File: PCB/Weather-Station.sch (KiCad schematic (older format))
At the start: 10 parts, among them J1 Biruta, J2 Power, J3 BH1750-FVI, J4 BME280, J5 Pluviometro, J6 Anamometro, U1 NodeMCU1.0(ESP-12E)

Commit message: Adicionando Gerber
Signed-off-by: Gustavo Costa <gustavocosta@ic.ufal.br>
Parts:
- J6: value Anamometro -> Anemometro
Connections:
- net labels added: +3.3V, +5V, GND
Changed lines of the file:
@@
 P 8150 3050
 F 0 "J6" H 8150 3150 50  0000 C CNN
-F 1 "Anamometro" H 8150 2850 50  0000 C CNN
+F 1 "Anemometro" H 8150 2850 50  0000 C CNN
 F 2 "Terminal_Blocks:TerminalBlock_Pheonix_MPT-2.54mm_2pol" H 8150 3050 50  0001 C CNN
 F 3 "" H 8150 3050 50  0001 C CNN
@@
 $EndComp
 Wire Wire Line
-	4900 3650 4250 3650
-Wire Wire Line
-	4250 3650 4250 2750
-Wire Wire Line
 	4250 2750 4000 2750
 Wire Wire Line
@@
 	6600 3950 6500 3950
 Wire Wire Line
-	6600 1400 6600 3950
-Wire Wire Line
 	6600 2950 7350 2950
 Wire Wire Line
@@
 Wire Wire Line
 	7100 3450 7100 3150
-Wire Wire Line
-	7950 1000 6700 1000
 Connection ~ 6700 1700
 Wire Wire Line
@@
 	7950 1200 6900 1200
 Connection ~ 6900 2000
-Wire Wire Line
-	7950 1400 6600 1400
 Connection ~ 6600 1800
 NoConn ~ 7950 1300
 Wire Wire Line
 	4550 3100 4550 3550
-Wire Wire Line
-	4550 3550 4900 3550
 NoConn ~ 4900 2750
 NoConn ~ 4900 2850
@@
 $Comp
 L PWR_FLAG #FLG01
-U 1 1 5A5912D8
-P 4350 3950
-F 0 "#FLG01" H 4350 4025 50  0001 C CNN
-F 1 "PWR_FLAG" H 4350 4100 50  0000 C CNN
-F 2 "" H 4350 3950 50  0001 C CNN
-F 3 "" H 4350 3950 50  0001 C CNN
-	1    4350 3950
-	1    0    0    -1
-$EndComp
-Wire Wire Line
-	4000 3950 4900 3950
-Connection ~ 4350 3950
-$Comp
-L PWR_FLAG #FLG02
 U 1 1 5A5913B0
 P 4350 4050
-F 0 "#FLG02" H 4350 4125 50  0001 C CNN
+F 0 "#FLG01" H 4350 4125 50  0001 C CNN
 F 1 "PWR_FLAG" H 4350 4200 50  0000 C CNN
 F 2 "" H 4350 4050 50  0001 C CNN
@@
 	-1   0    0    1
 $EndComp
-Wire Wire Line
-	4000 4050 4900 4050
-Connection ~ 4350 4050
 $Comp
 L R R1
@@
 Connection ~ 7350 3150
 Connection ~ 7350 2650
+$Comp
+L GND #PWR02
+U 1 1 5A5CDF65
+P 4700 3950
+F 0 "#PWR02" H 4700 3700 50  0001 C CNN
+F 1 "GND" H 4700 3800 50  0000 C CNN
+F 2 "" H 4700 3950 50  0001 C CNN
+F 3 "" H 4700 3950 50  0001 C CNN
+	1    4700 3950
+	-1   0    0    1
+$EndComp
+$Comp
+L GND #PWR03
+U 1 1 5A5CDF8D
+P 4700 3550
+F 0 "#PWR03" H 4700 3300 50  0001 C CNN
+F 1 "GND" H 4700 3400 50  0000 C CNN
+F 2 "" H 4700 3550 50  0001 C CNN
+F 3 "" H 4700 3550 50  0001 C CNN
+	1    4700 3550
+	-1   0    0    1
+$EndComp
+Wire Wire Line
+	4550 3550 4900 3550
+Connection ~ 4700 3550
+$Comp
+L PWR_FLAG #FLG04
+U 1 1 5A5912D8
+P 4350 3950
+F 0 "#FLG04" H 4350 4025 50  0001 C CNN
+F 1 "PWR_FLAG" H 4350 4100 50  0000 C CNN
+F 2 "" H 4350 3950 50  0001 C CNN
+F 3 "" H 4350 3950 50  0001 C CNN
+	1    4350 3950
+	1    0    0    -1
+$EndComp
+Wire Wire Line
+	4000 3950 4900 3950
+Connection ~ 4350 3950
+Connection ~ 4700 3950
+$Comp
+L GND #PWR05
+U 1 1 5A5CE28B
+P 6600 1400
+F 0 "#PWR05" H 6600 1150 50  0001 C CNN
+F 1 "GND" H 6600 1250 50  0000 C CNN
+F 2 "" H 6600 1400 50  0001 C CNN
+F 3 "" H 6600 1400 50  0001 C CNN
+	1    6600 1400
+	0    1    1    0
+$EndComp
+Wire Wire Line
+	6600 1400 6600 3950
+Wire Wire Line
+	7950 1400 6600 1400
+$Comp
+L +3.3V #PWR06
+U 1 1 5A5CE575
+P 4400 3650
+F 0 "#PWR06" H 4400 3500 50  0001 C CNN
+F 1 "+3.3V" H 4400 3790 50  0000 C CNN
+F 2 "" H 4400 3650 50  0001 C CNN
+F 3 "" H 4400 3650 50  0001 C CNN
+	1    4400 3650
+	1    0    0    -1
+$EndComp
+Wire Wire Line
+	4250 3650 4900 3650
+Connection ~ 4400 3650
+$Comp
+L +3.3V #PWR07
+U 1 1 5A5CE693
+P 6700 1000
+F 0 "#PWR07" H 6700 850 50  0001 C CNN
+F 1 "+3.3V" H 6700 1140 50  0000 C CNN
+F 2 "" H 6700 1000 50  0001 C CNN
+F 3 "" H 6700 1000 50  0001 C CNN
+	1    6700 1000
+	0    -1   -1   0
+$EndComp
+Wire Wire Line
+	7950 1000 6700 1000
+$Comp
+L +5V #PWR08
+U 1 1 5A5CE7AA
+P 4700 4050
+F 0 "#PWR08" H 4700 3900 50  0001 C CNN
+F 1 "+5V" H 4700 4190 50  0000 C CNN
+F 2 "" H 4700 4050 50  0001 C CNN
+F 3 "" H 4700 4050 50  0001 C CNN
+	1    4700 4050
+	-1   0    0    1
+$EndComp
+Wire Wire Line
+	4000 4050 4900 4050
+Connection ~ 4350 4050
+Connection ~ 4700 4050
+$Comp
+L PWR_FLAG #FLG09
+U 1 1 5A5CE960
+P 4250 3300
+F 0 "#FLG09" H 4250 3375 50  0001 C CNN
+F 1 "PWR_FLAG" H 4250 3450 50  0000 C CNN
+F 2 "" H 4250 3300 50  0001 C CNN
+F 3 "" H 4250 3300 50  0001 C CNN
+	1    4250 3300
+	0    -1   -1   0
+$EndComp
+Wire Wire Line
+	4250 2750 4250 3650
+Connection ~ 4250 3300
 $EndSCHEMATC

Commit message: Refazendo PCB
Signed-off-by: Gustavo Costa <gustavocosta@ic.ufal.br>
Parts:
- removed U1: NodeMCU1.0(ESP-12E), ESP8266_l2:NodeMCU1.0(12-E), symbol NodeMCU1.0(ESP-12E)
- added C1: 100nF, Capacitors_SMD:C_0805, symbol C
- added J7: FTDI, Pin_Headers:Pin_Header_Straight_1x04_Pitch2.54mm, symbol Conn_01x04
- added R4, R5, R6, R7, R8: 10K, Resistors_SMD:R_0805, symbol R
- added SW1: SW_Push_SPDT, Buttons_Switches_ThroughHole:SW_Micro_SPST, symbol SW_Push_SPDT
- added SW2: SW_Push, Buttons_Switches_THT:SW_PUSH_6mm, symbol SW_Push
- added SW3: SW_DIP_x01, Buttons_Switches_ThroughHole:SW_Micro_SPST, symbol SW_DIP_x01
- added U1: AP1117-33, TO_SOT_Packages_SMD:SOT-223-3_TabPin2, symbol AP1117-33
- added U2: ESP-12E, ESP8266:ESP-12E, symbol ESP-12E
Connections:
- net labels added: RXD, TXD
- net labels removed: +5V
- wire segments 38 -> 89
- no-connect marks 20 -> 9
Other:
- moved on the sheet: J1, J2, J3, J4, J5, J6, R1, R2, R3

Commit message: Ajustando os valores da biruta
Signed-off-by: Gustavo Costa <gustavocosta@ic.ufal.br>
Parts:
- U1: footprint TO_SOT_Packages_SMD:SOT-223-3_TabPin2 -> TO_SOT_Packages_SMD:SOT-223
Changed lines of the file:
@@
 F 0 "U1" H 2000 2775 50  0000 C CNN
 F 1 "AP1117-33" H 2150 2775 50  0000 L CNN
-F 2 "TO_SOT_Packages_SMD:SOT-223-3_TabPin2" H 2150 2850 50  0001 C CNN
+F 2 "TO_SOT_Packages_SMD:SOT-223" H 2150 2850 50  0001 C CNN
 F 3 "" H 2250 2400 50  0001 C CNN
 	1    2150 2650

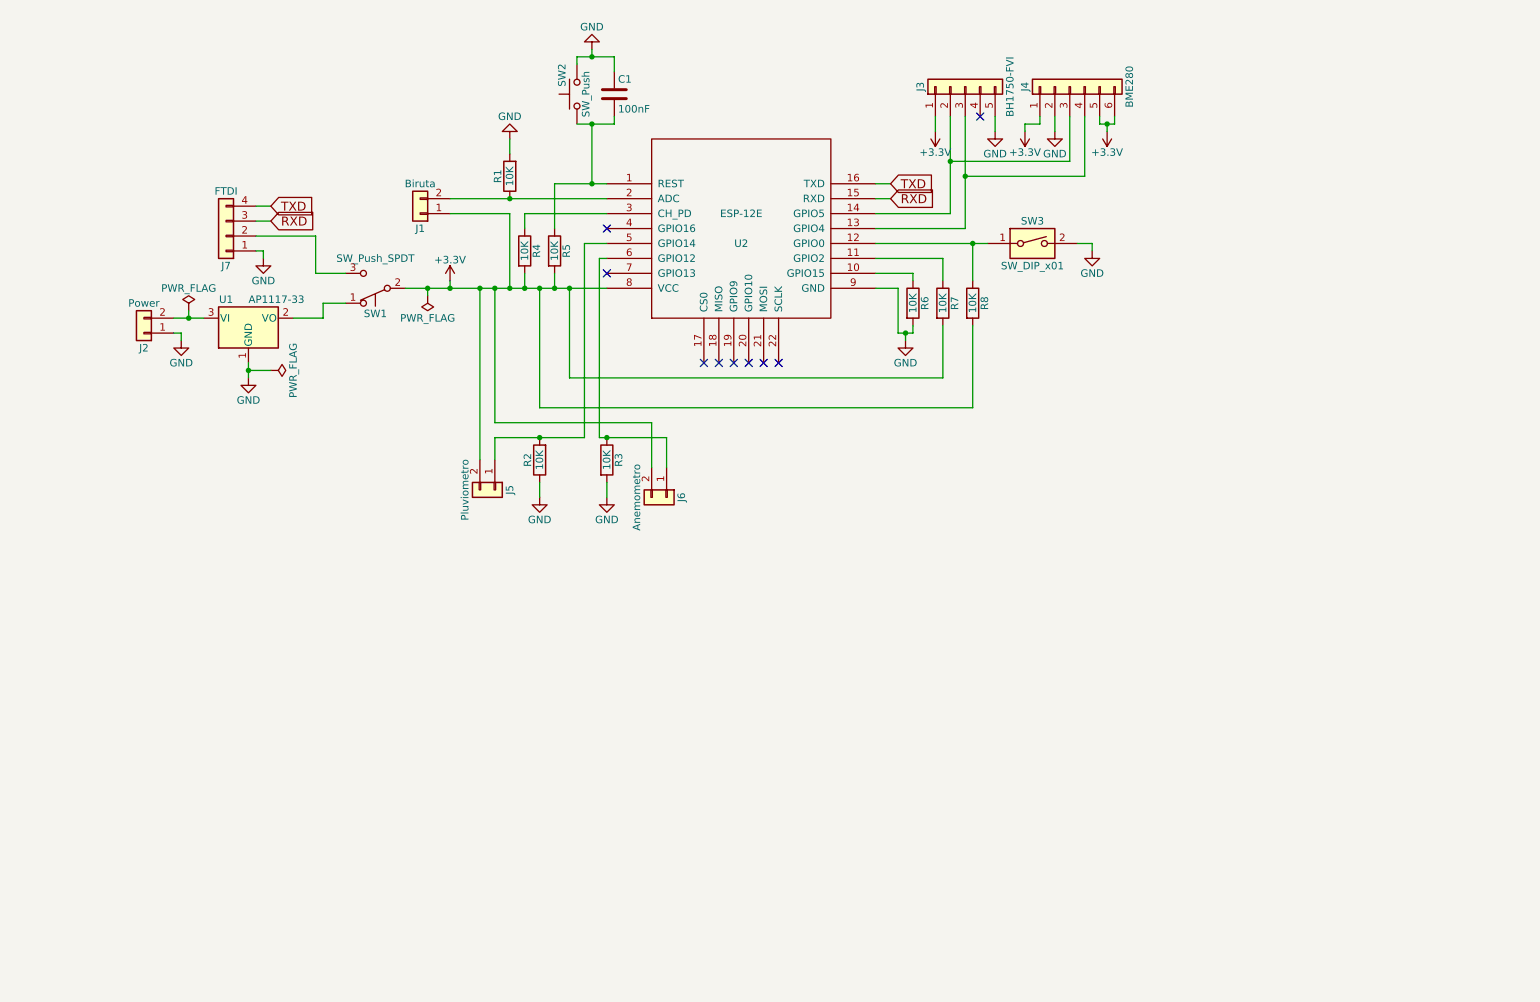
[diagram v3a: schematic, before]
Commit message: Iniciada a PCB com ESP32 devkit
Signed-off-by: Gustavo Costa <gustavocosta@ic.ufal.br>
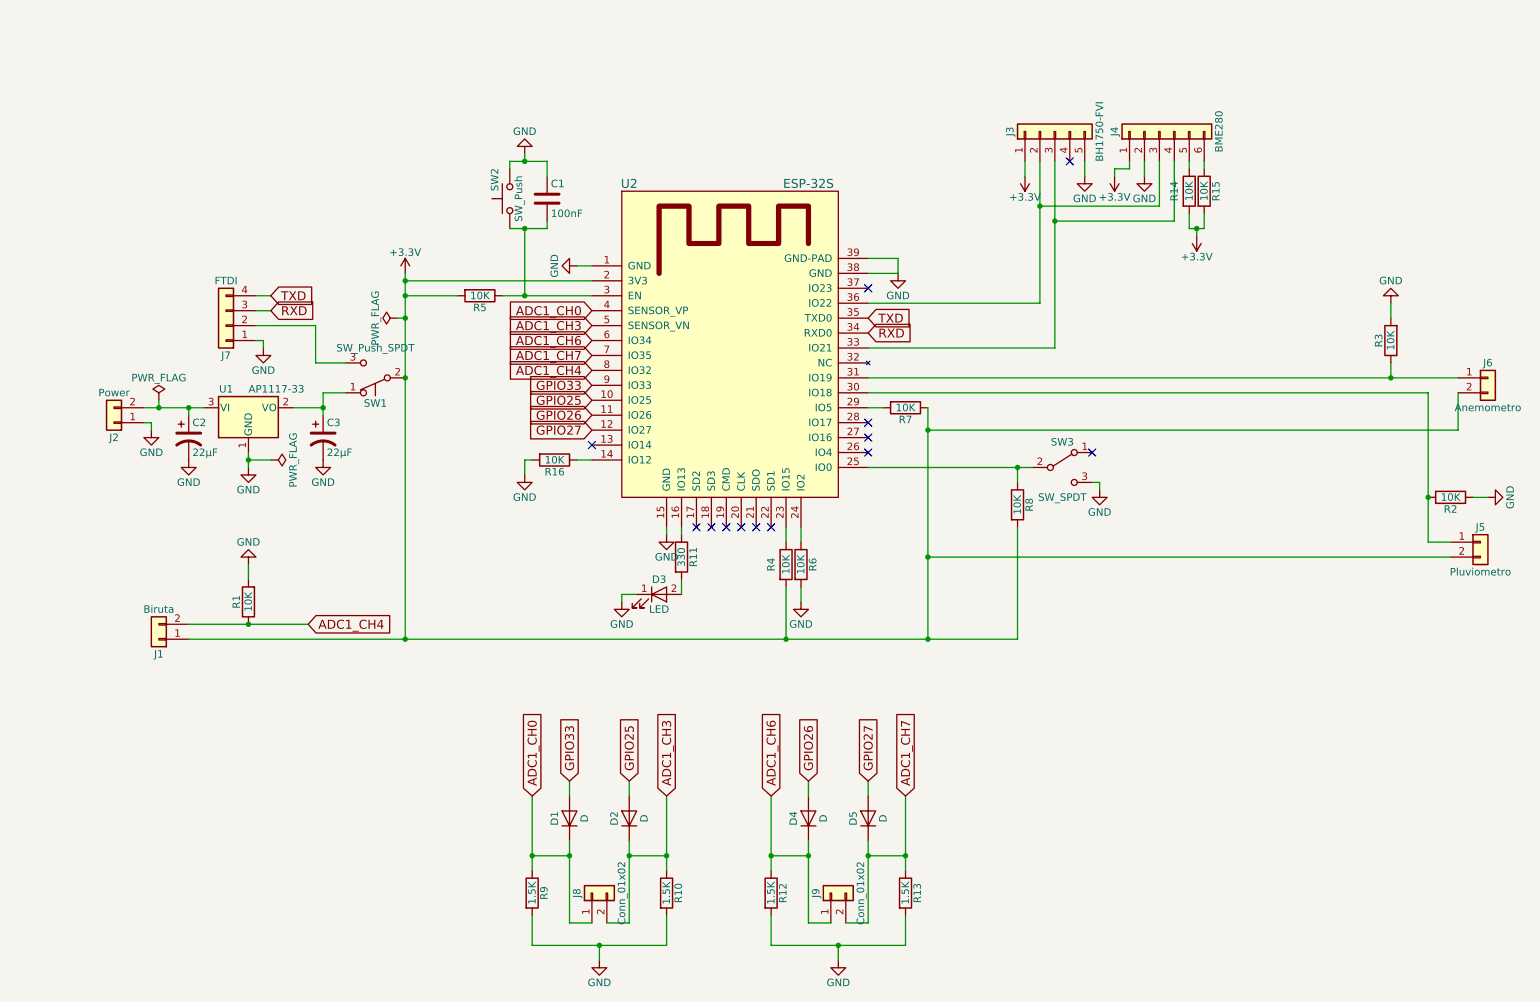
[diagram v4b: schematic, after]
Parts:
- removed SW3: SW_DIP_x01, Buttons_Switches_ThroughHole:SW_Micro_SPST, symbol SW_DIP_x01
- removed U2: ESP-12E, ESP8266:ESP-12E, symbol ESP-12E
- added C2, C3: 22μF, Capacitors_SMD:CP_Elec_6.3x7.7, symbol CP1
- added D1, D2, D4, D5: D, Diodes_SMD:D_SOD-123, symbol D
- added D3: LED, LEDs:LED_0805, symbol LED
- added J8, J9: Conn_01x02, TerminalBlock_Phoenix:TerminalBlock_Phoenix_MPT-2.54mm_2pol, symbol Conn_01x02
- added R10, R12, R13, R9: 1.5K, Resistors_SMD:R_0805, symbol R
- added R11: 330, Resistors_SMD:R_0805, symbol R
- added R14, R15, R16: 10K, Resistors_SMD:R_0805, symbol R
- added SW3: SW_SPDT, Buttons_Switches_ThroughHole:SW_Micro_SPST, symbol SW_SPDT
- added U2: ESP-32S, MPPT_Library:ESP32-WROOM, symbol ESP-32S
- J1, J2, J5, J6: footprint Terminal_Blocks:TerminalBlock_Pheonix_MPT-2.54mm_2pol -> TerminalBlock_Phoenix:TerminalBlock_Phoenix_MPT-2.54mm_2pol
- J3: footprint Terminal_Blocks:TerminalBlock_Pheonix_MPT-2.54mm_5pol -> TerminalBlock_Phoenix:TerminalBlock_Phoenix_MPT-2.54mm_5pol
- J4: footprint Terminal_Blocks:TerminalBlock_Pheonix_MPT-2.54mm_6pol -> TerminalBlock_Phoenix:TerminalBlock_Phoenix_MPT-2.54mm_6pol
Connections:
- net +3V3: now also R7.1, R14.2, R15.2, U2.2 (3V3); no longer J4.5 (Pin_5), J4.6 (Pin_6), R7.2
- net GND: now also C2.2, C3.2, D3.1 (K), R10.2, R12.2, R13.2, R16.2, R9.2, SW3.3 (C), U2.1 (GND), U2.15 (GND), U2.38 (GND), U2.39 (GND-PAD)
- net RXD: now also U2.34 (RXD0)
- net TXD: now also U2.35 (TXD0)
- net at J6.1 (Pin_1), R3.1: now also U2.31 (IO19)
- net at J5.1 (Pin_1), R2.2: now also U2.30 (IO18)
- net ADC1_CH4: now reaches J1.2 (Pin_2), R1.1
- net ADC1_CH4: now also U2.8 (IO32)
- net at J3.2 (Pin_2), J4.3 (Pin_3): now also U2.36 (IO22)
- net at J3.3 (Pin_3), J4.4 (Pin_4): now also U2.33 (IO21)
- net at J2.2 (Pin_2), U1.3 (VI): now also C2.1
- net at C1.2, R5.1, SW2.1: now also U2.3 (EN)
- net at R6.1: now also U2.24 (IO2)
- net at R8.1: now also SW3.2 (B), U2.25 (IO0)
- net at R4.1: now also U2.23 (IO15)
- net at SW1.1 (A), U1.2 (VO): now also C3.1
- new net: J4.5 (Pin_5), R14.1
- new net: J4.6 (Pin_6), R15.1
- new net: R7.2, U2.29 (IO5)
- new net: R16.1, U2.14 (IO12)
- new net: R11.1, U2.16 (IO13)
- new net: D3.2 (A), R11.2
- new net ADC1_CH0: D1.1 (K), J8.1 (Pin_1), R9.1, U2.4 (SENSOR_VP)
- new net ADC1_CH3: D2.1 (K), J8.2 (Pin_2), R10.1, U2.5 (SENSOR_VN)
- new net ADC1_CH6: D4.1 (K), J9.1 (Pin_1), R12.1, U2.6 (IO34)
- new net ADC1_CH7: D5.1 (K), J9.2 (Pin_2), R13.1, U2.7 (IO35)
- new net GPIO25: D2.2 (A), U2.10 (IO25)
- new net GPIO26: D4.2 (A), U2.11 (IO26)
- new net GPIO27: D5.2 (A), U2.12 (IO27)
- new net GPIO33: D1.2 (A), U2.9 (IO33)
- no-connect marks 9 -> 13
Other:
- moved on the sheet: C1, J1, J2, J3, J4, J5, J6, J7, R1, R2, R3, R4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

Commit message: Alterando as PCBs da estação para usar os ADCs e o DataLogger
Signed-off-by: Gustavo Costa <gustavocosta@ic.ufal.br>
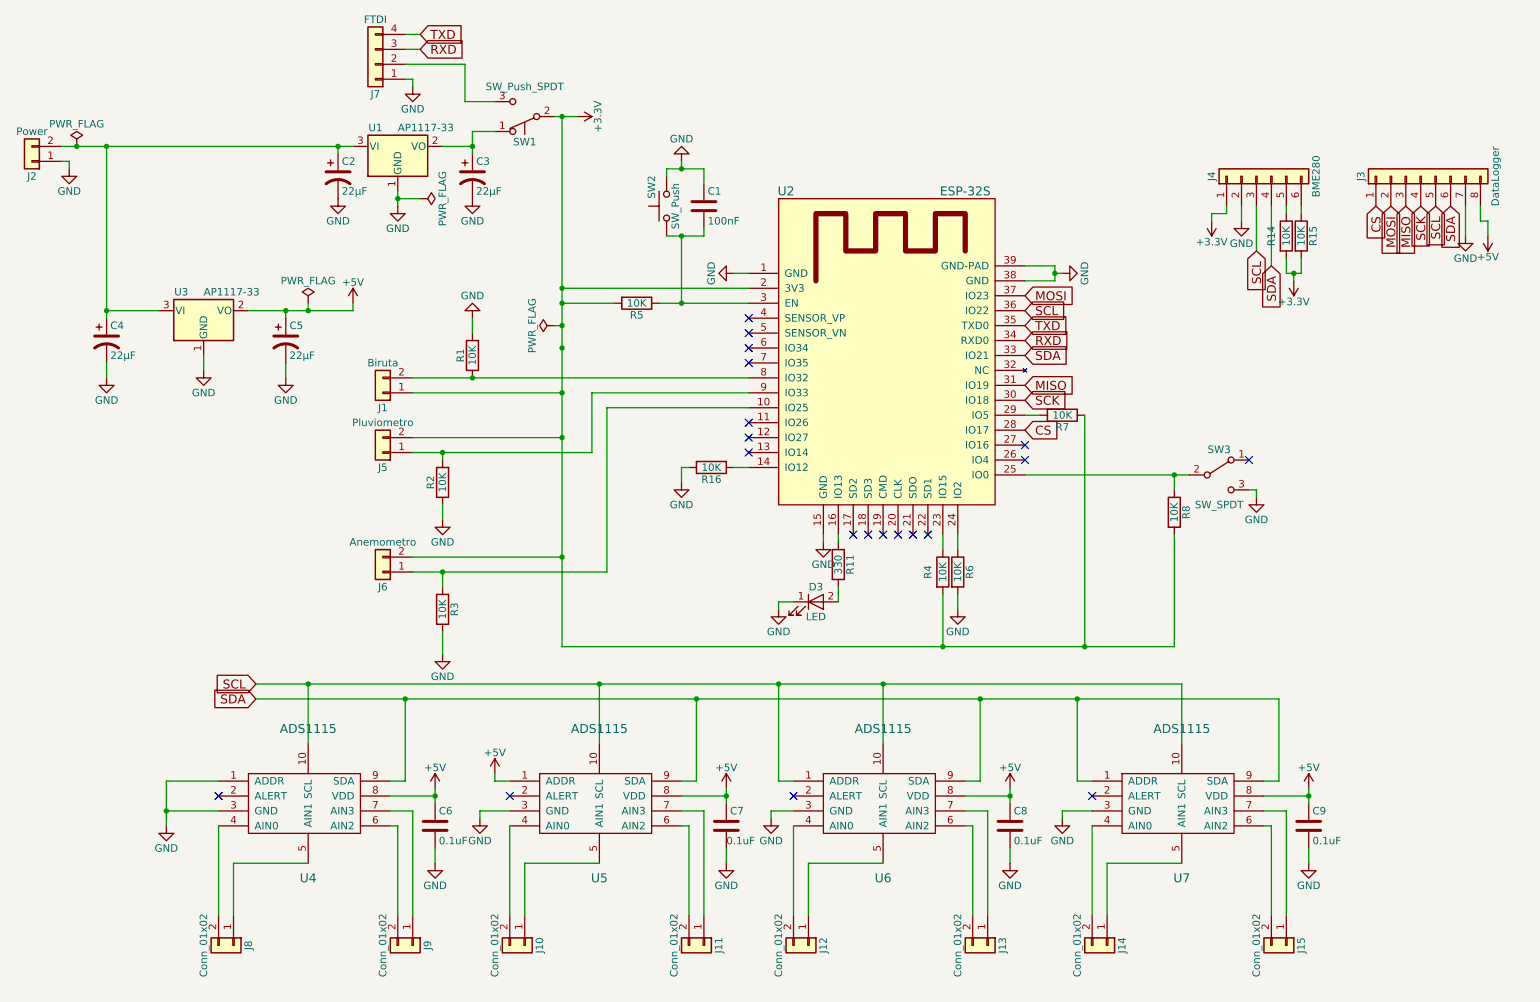
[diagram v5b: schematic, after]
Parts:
- removed D1, D2, D4, D5: D, Diodes_SMD:D_SOD-123, symbol D
- removed J3: BH1750-FVI, TerminalBlock_Phoenix:TerminalBlock_Phoenix_MPT-2.54mm_5pol, symbol Conn_01x05
- removed R10, R12, R13, R9: 1.5K, Resistors_SMD:R_0805, symbol R
- added C4, C5: 22μF, Capacitors_SMD:CP_Elec_6.3x7.7, symbol CP1
- added C6, C7, C8, C9: 0.1uF, Capacitors_SMD:C_0805, symbol C
- added J10, J11, J12, J13, J14, J15: Conn_01x02, TerminalBlock_Phoenix:TerminalBlock_Phoenix_MPT-2.54mm_2pol, symbol Conn_01x02
- added J3: DataLogger, Pin_Headers:Pin_Header_Straight_1x08_Pitch2.54mm, symbol Conn_01x08
- added U3: AP1117-33, TO_SOT_Packages_SMD:SOT-223-3Lead_TabPin2, symbol AP1117-33
- added U4, U5, U6, U7: ADS1115, Housings_SSOP:MSOP-10_3x3mm_Pitch0.5mm, symbol ADS1115
- J2: footprint TerminalBlock_Phoenix:TerminalBlock_Phoenix_MPT-2.54mm_2pol -> TerminalBlock_Phoenix:TerminalBlock_Phoenix_PT-3.5mm_2pol
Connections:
- net GPIO25 is gone; now on an unnamed net: U2.10 (IO25)
- net GPIO33 is gone; now on an unnamed net: U2.9 (IO33)
- net GND: now also C4.2, C5.2, C6.2, C7.2, C8.2, C9.2, J3.7 (Pin_7), U3.1 (GND), U4.1 (ADDR), U4.3 (GND), U5.3 (GND), U6.3 (GND), U7.3 (GND)
- net at J6.1 (Pin_1), R3.1: no longer U2.31 (IO19)
- net at J5.1 (Pin_1), R2.2: no longer U2.30 (IO18)
- net SCL: now reaches J4.3 (Pin_3), U2.36 (IO22)
- net SCL: now also J3.5 (Pin_5), U4.10 (SCL), U5.10 (SCL), U6.1 (ADDR), U6.10 (SCL), U7.10 (SCL)
- net SDA: now reaches J4.4 (Pin_4), U2.33 (IO21)
- net SDA: now also J3.6 (Pin_6), U4.9 (SDA), U5.9 (SDA), U6.9 (SDA), U7.1 (ADDR), U7.9 (SDA)
- net at C2.1, J2.2 (Pin_2), U1.3 (VI): now also C4.1, U3.3 (VI)
- net CS: now reaches U2.28 (IO17)
- net CS: now also J3.1 (Pin_1)
- net MOSI: now reaches U2.37 (IO23)
- net MOSI: now also J3.2 (Pin_2)
- net ADC1_CH0: no longer names the net of U2.4 (SENSOR_VP)
- net ADC1_CH0: no longer J8.1 (Pin_1)
- net ADC1_CH3: no longer names the net of U2.5 (SENSOR_VN)
- net ADC1_CH3: no longer J8.2 (Pin_2)
- net ADC1_CH4: no longer names the net of J1.2 (Pin_2), R1.1, U2.8 (IO32)
- net ADC1_CH6: no longer names the net of U2.6 (IO34)
- net ADC1_CH6: no longer J9.1 (Pin_1)
- net ADC1_CH7: no longer names the net of U2.7 (IO35)
- net ADC1_CH7: no longer J9.2 (Pin_2)
- net GPIO26: no longer names the net of U2.11 (IO26)
- net GPIO27: no longer names the net of U2.12 (IO27)
- new net: J8.2 (Pin_2), U4.4 (AIN0)
- new net: J8.1 (Pin_1), U4.5 (AIN1)
- new net: J9.2 (Pin_2), U4.6 (AIN2)
- new net: J9.1 (Pin_1), U4.7 (AIN3)
- new net: J10.2 (Pin_2), U5.4 (AIN0)
- new net: J10.1 (Pin_1), U5.5 (AIN1)
- new net: J11.2 (Pin_2), U5.6 (AIN2)
- new net: J11.1 (Pin_1), U5.7 (AIN3)
- new net: J12.2 (Pin_2), U6.4 (AIN0)
- new net: J12.1 (Pin_1), U6.5 (AIN1)
- new net: J13.2 (Pin_2), U6.6 (AIN2)
- new net: J13.1 (Pin_1), U6.7 (AIN3)
- new net: J14.2 (Pin_2), U7.4 (AIN0)
- new net: J14.1 (Pin_1), U7.5 (AIN1)
- new net: J15.2 (Pin_2), U7.6 (AIN2)
- new net: J15.1 (Pin_1), U7.7 (AIN3)
- new net +5V: C5.1, C6.1, C7.1, C8.1, C9.1, J3.8 (Pin_8), U3.2 (VO), U4.8 (VDD), U5.1 (ADDR), U5.8 (VDD), U6.8 (VDD), U7.8 (VDD)
- new net MISO: J3.3 (Pin_3), U2.31 (IO19)
- new net SCK: J3.4 (Pin_4), U2.30 (IO18)
- no-connect marks 13 -> 20
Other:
- moved on the sheet: C1, C2, C3, D3, J1, J2, J4, J5, J6, J7, R1, R11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

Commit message: Iniciado PCB
Signed-off-by: Gustavo Costa <gustavocosta@ic.ufal.br>
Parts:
- U3: footprint TO_SOT_Packages_SMD:SOT-223-3Lead_TabPin2 -> TO_SOT_Packages_SMD:SOT-223
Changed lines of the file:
@@
 F 0 "U3" H 1700 2725 50  0000 C CNN
 F 1 "AP1117-33" H 1850 2725 50  0000 L CNN
-F 2 "TO_SOT_Packages_SMD:SOT-223-3Lead_TabPin2" H 1850 2800 50  0001 C CNN
+F 2 "TO_SOT_Packages_SMD:SOT-223" H 1850 2800 50  0001 C CNN
 F 3 "" H 1950 2350 50  0001 C CNN
 	1    1850 2600
